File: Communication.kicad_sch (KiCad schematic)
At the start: 44 parts

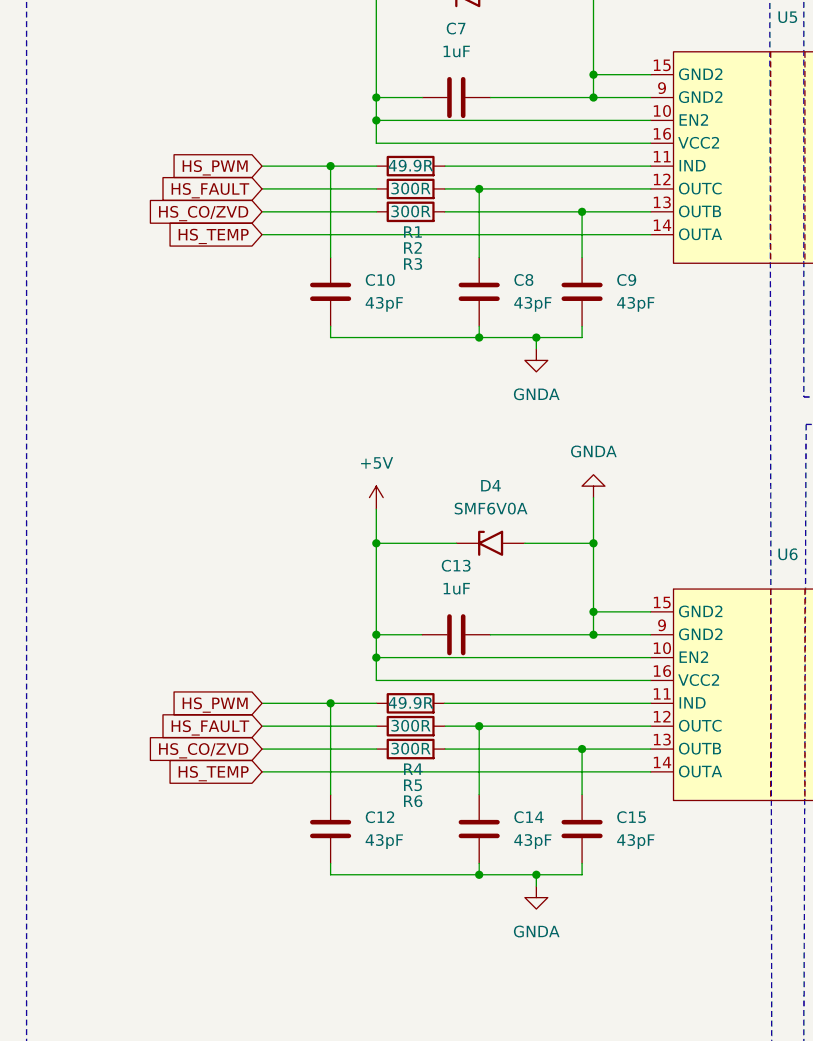
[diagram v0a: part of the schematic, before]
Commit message: added vias
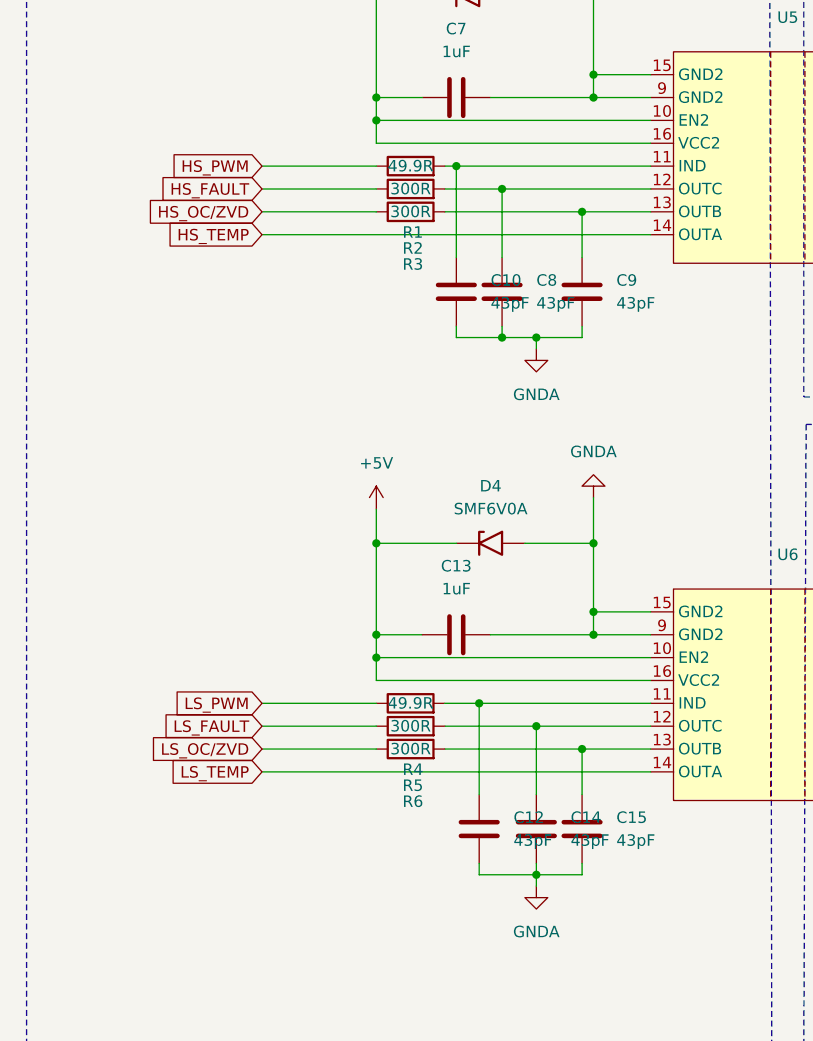
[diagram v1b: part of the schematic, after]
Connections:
- net HS_FAULT: no longer R5.1
- net HS_PWM: no longer C10.2, C12.2, R4.1
- net HS_TEMP: no longer U6.14 (OUTA)
- net at R1.2, U5.11 (IND): now also C10.2
- net at R4.2, U6.11 (IND): now also C12.2
- net HS_CO/ZVD renamed HS_OC/ZVD
- net HS_OC/ZVD: no longer R6.1
- new net LS_FAULT: R5.1
- new net LS_OC/ZVD: R6.1
- new net LS_PWM: R4.1
- new net LS_TEMP: U6.14 (OUTA)
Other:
- moved on the sheet: C10, C12, C14, C8
